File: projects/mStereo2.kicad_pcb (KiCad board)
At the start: 4 copper layers, 159.5 x 120 mm, 125 parts, among them P101 CONN_AMANERO, P102 Screw-term 1x2, P103 Screw-term 1X3, P104 XLR-MALE, P105 XLR-MALE, U101 ISO7640, U102 CDCLVC1104, U103 MCP100-315DI, U104 SRC4192, U201 LT1761, U301 WM8741, U401 WM8741, U501 LT1763, U601 OPA1632, U602 OPA1632, U701 OPA1632, U702 OPA1632, X101 XTAL

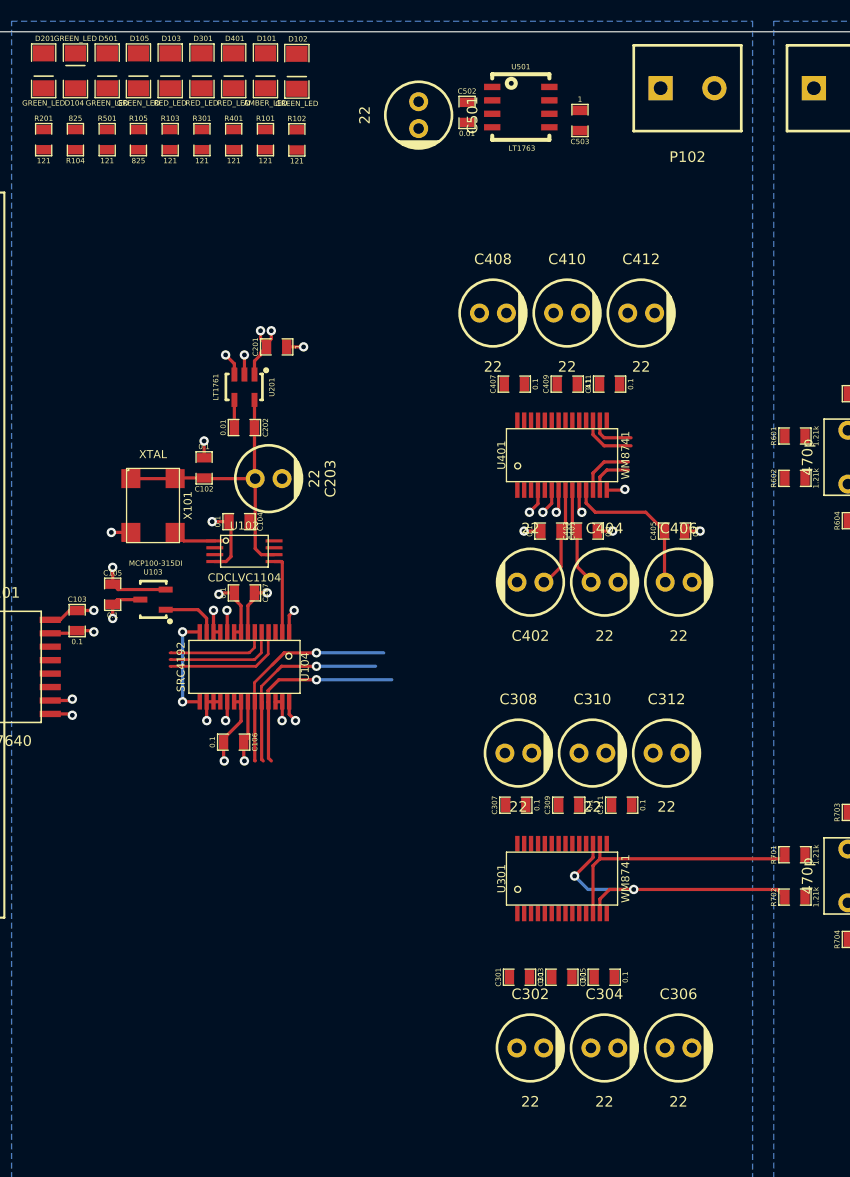
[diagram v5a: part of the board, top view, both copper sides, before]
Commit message: more routing: reached about 50% completion
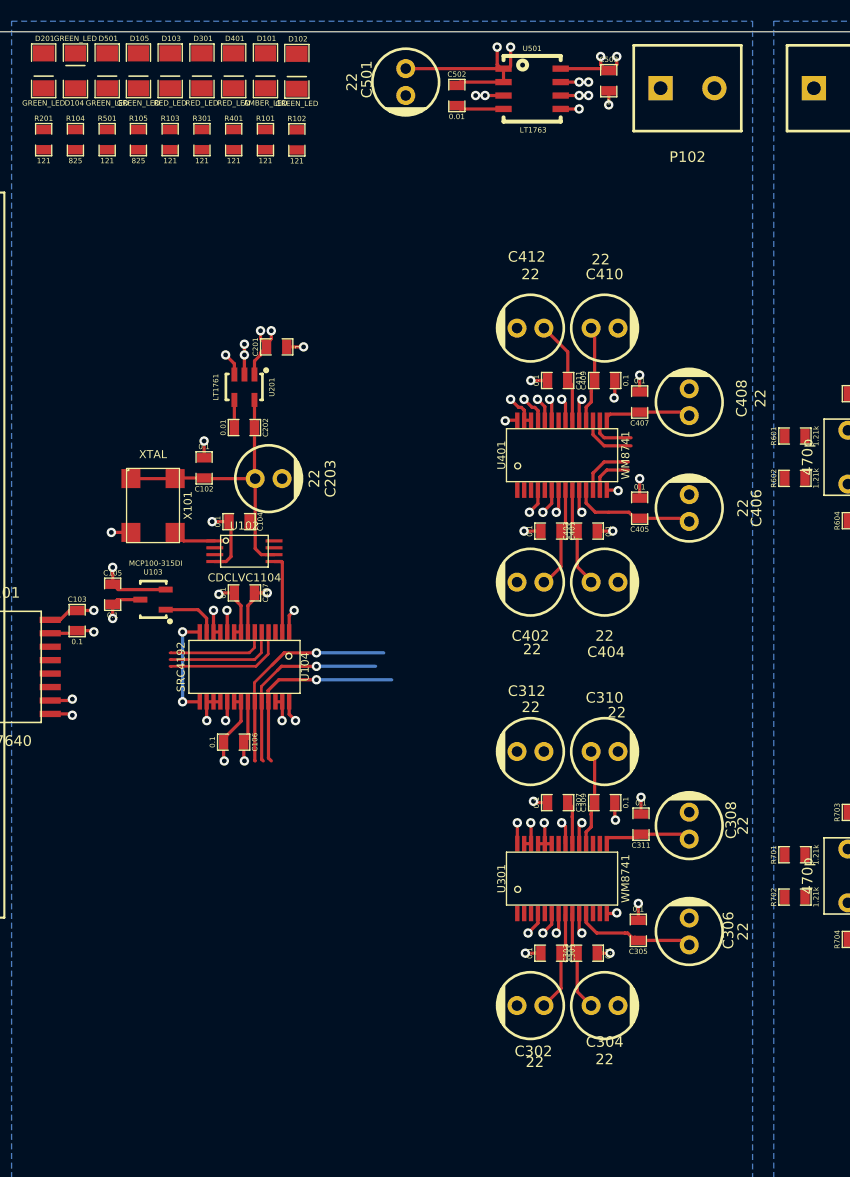
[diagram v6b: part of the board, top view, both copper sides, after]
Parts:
- moved C408 20.4 mm to (137.0, 70.0), turned to 90 degrees
- moved C308 17.5 mm to (137.0, 110.0), turned to 90 degrees
- moved C312 12.9 mm to (122.0, 103.0), turned to 180 degrees
- moved C407 12.0 mm to (132.3, 70.0), turned to 90 degrees
- moved C306 11.1 mm to (137.0, 120.0), turned to 90 degrees
- moved C412 10.6 mm to (122.0, 63.0), turned to 180 degrees
- moved C406 7.07 mm to (137.0, 80.0), turned to 90 degrees
- moved C305 5.48 mm to (132.2, 119.9), turned to 90 degrees
- moved C411 4.92 mm to (124.6, 67.9), turned to 180 degrees
- moved C503 4.64 mm to (129.4, 39.6), turned to 270 degrees
- moved C302 4.00 mm to (122.0, 127.0), turned to 180 degrees
- moved C304 4.00 mm to (129.0, 127.0)
- moved C307 3.96 mm to (124.6, 107.8), turned to 180 degrees
- moved C405 3.95 mm to (132.3, 80.0), turned to 90 degrees
- moved C410 3.82 mm to (129.0, 63.0)
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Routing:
- net +5V: track 18.1 -> 68.4 mm, vias 3 -> 6
- net DGND: track 60.5 -> 104.2 mm, vias 21 -> 47
- net VDD: track 42.9 -> 85.9 mm, vias 9 -> 17
- net /FILTER_R/VIN-: track 29.4 -> 0.00 mm, vias 2 -> 0
- net /FILTER_R/VIN+: track 24.5 -> 0.00 mm
- net Net-(C305-Pad1): track 0.00 -> 11.9 mm
- net Net-(C309-Pad1): track 0.00 -> 9.30 mm
- net Net-(C409-Pad1): track 0.00 -> 9.18 mm
- net Net-(C502-Pad2): track 0.00 -> 4.55 mm
- net Net-(C405-Pad1): track 14.6 -> 11.7 mm
- net Net-(D401-Pad1): track 0.00 -> 2.13 mm, vias 0 -> 1
- net Net-(D301-Pad1): track 0.00 -> 2.12 mm, vias 0 -> 1

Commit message: more routing; reached 75% completion
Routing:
- net /DAC_L/BCLK: track 18.9 -> 82.1 mm, vias 1 -> 2
- net /DAC_L/DATA: track 20.9 -> 81.6 mm, vias 1 -> 2
- net /DAC_R/MCLK: track 0.00 -> 48.5 mm
- net /DAC_L/LRCLK: track 18.7 -> 55.6 mm, vias 1 -> 2
- net /DAC_L/MCLK: track 0.00 -> 33.8 mm
- net /LRCLK_1: track 58.6 -> 45.0 mm
- net /BCLK_1: track 60.4 -> 47.3 mm
- net /DATA_1: track 62.3 -> 49.7 mm
- net /DATA_2: track 11.8 -> 23.7 mm
- net /BCLK_2: track 10.8 -> 22.1 mm
- net /LRCLK_2: track 9.61 -> 20.6 mm
- net +5V: track 68.4 -> 74.1 mm

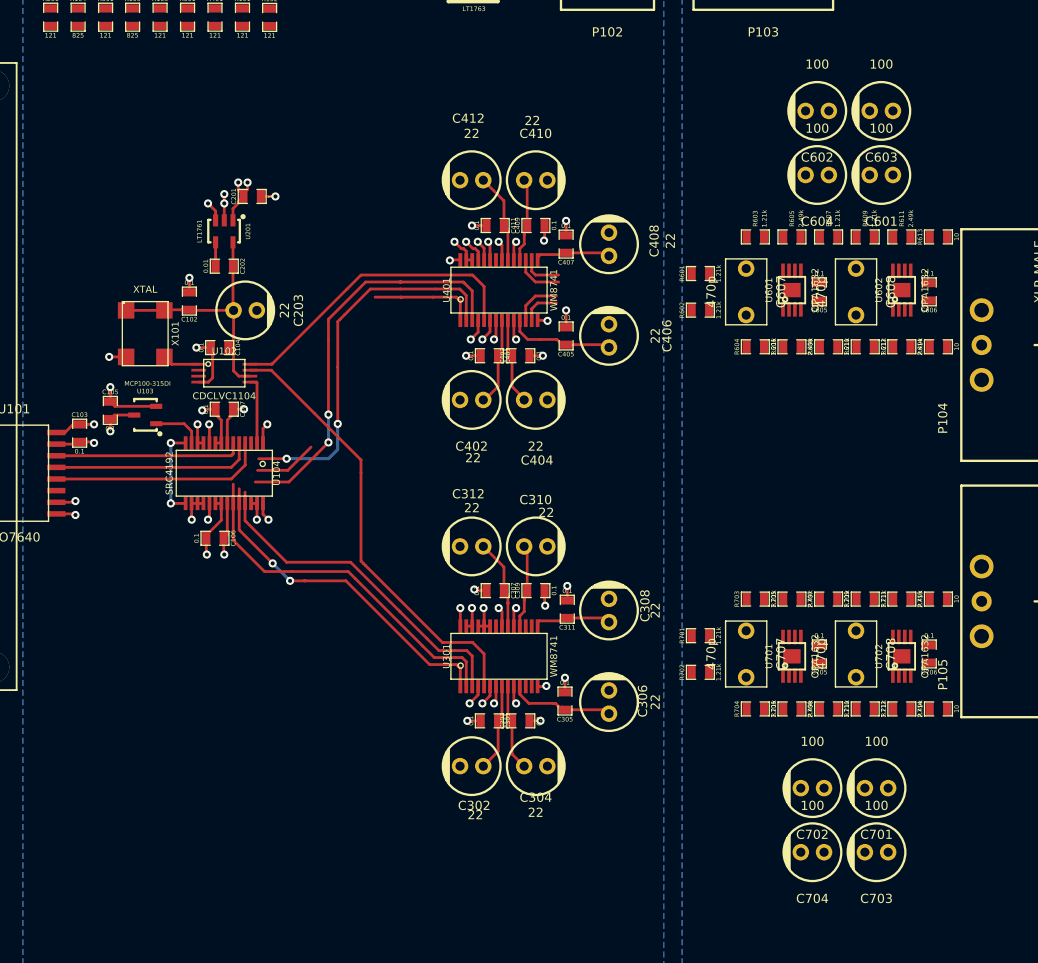
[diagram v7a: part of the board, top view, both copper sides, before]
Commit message: more routing and component placement revision
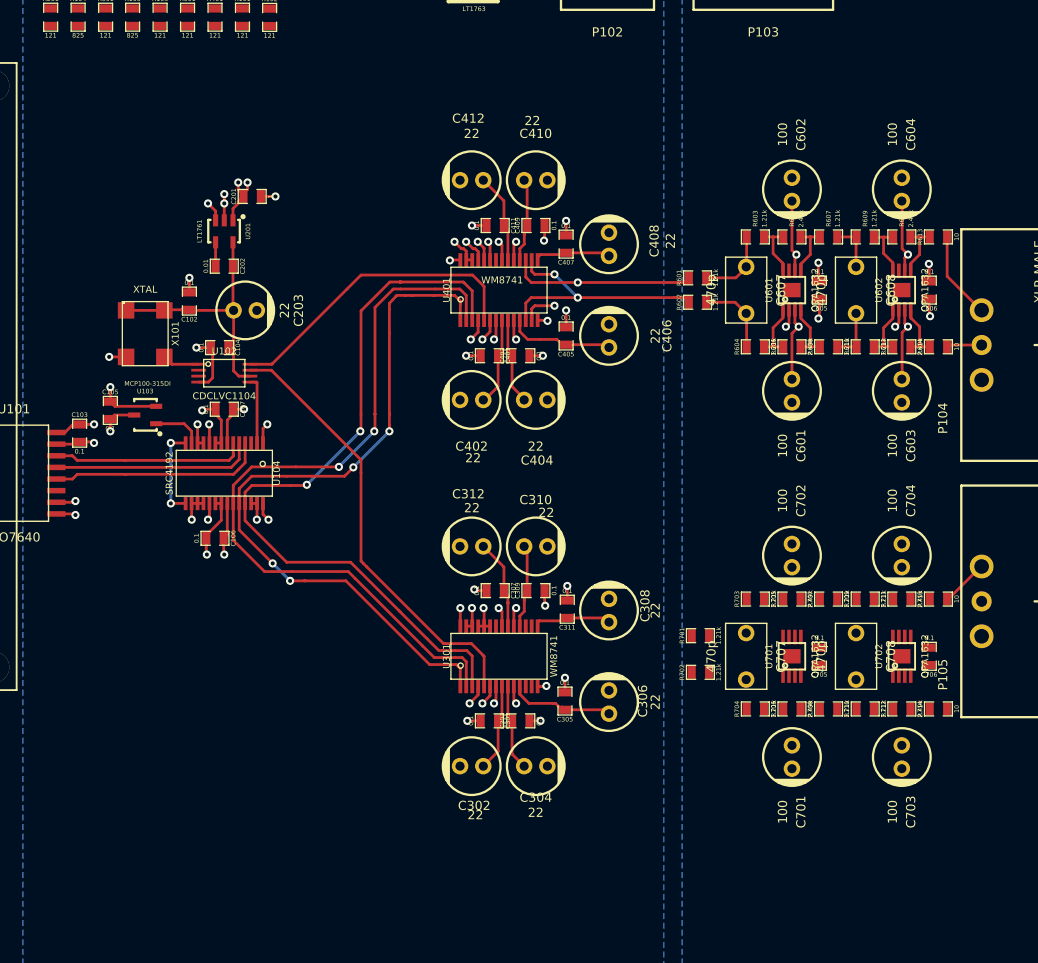
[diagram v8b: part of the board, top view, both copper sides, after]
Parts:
- moved C704 33.8 mm to (169.0, 104.0), turned to 270 degrees
- moved C603 30.7 mm to (169.0, 86.0), turned to 270 degrees
- moved C601 25.5 mm to (157.0, 86.0), turned to 270 degrees
- moved C702 25.5 mm to (157.0, 104.0), turned to 270 degrees
- moved C703 10.8 mm to (169.0, 126.0), turned to 270 degrees
- moved C701 9.84 mm to (157.0, 126.0), turned to 270 degrees
- moved C604 9.37 mm to (169.0, 64.0), turned to 270 degrees
- moved C602 9.01 mm to (157.0, 64.0), turned to 270 degrees
- moved R602 0.92 mm to (146.7, 76.3)
- moved R601 0.57 mm to (146.7, 73.7)
- moved C705 0.25 mm to (160.0, 115.0)
- moved C706 0.25 mm to (172.0, 115.0)
- moved C707 0.25 mm to (152.0, 115.0)
- moved C708 0.25 mm to (164.0, 115.0)
- moved C605 0.19 mm to (160.0, 75.0)
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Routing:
- net +12V: track 0.00 -> 25.7 mm, vias 0 -> 4
- net -12V: track 0.00 -> 25.4 mm, vias 0 -> 4
- net /DAC_L/LRCLK: track 55.6 -> 80.7 mm, vias 2 -> 4
- net /FILTER_L/VIN+: track 9.59 -> 27.6 mm, vias 0 -> 2
- net /FILTER_L/VIN-: track 9.74 -> 27.6 mm, vias 0 -> 2
- net /FILTER_L/VOUT+: track 0.00 -> 9.60 mm
- net Net-(C607-Pad2): track 0.00 -> 8.53 mm
- net Net-(C607-Pad1): track 0.00 -> 8.19 mm
- net Net-(R606-Pad2): track 0.00 -> 6.69 mm
- net Net-(R604-Pad2): track 0.00 -> 6.63 mm
- net Net-(R610-Pad2): track 0.00 -> 6.62 mm
- net Net-(R612-Pad2): track 0.00 -> 6.59 mm
- net Net-(R605-Pad2): track 0.00 -> 6.54 mm
- net Net-(R609-Pad2): track 0.00 -> 6.35 mm
- net Net-(R603-Pad2): track 0.00 -> 6.25 mm
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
